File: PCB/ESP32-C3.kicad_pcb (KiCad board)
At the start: 2 copper layers, 29.1 x 19.5 mm, 41 parts, among them J1 BattConn+, J2 BattConn-, SW1 TAK_6mm_THT, U1 USB-C-16P-SMD, U2 XT4052K421MR-G, U3 ESP32-C3, U4 RS3236-3.3YF5, X1 DPS_I2C, Y1 40MHz_S3240000151040

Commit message: gerber erstellt
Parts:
- X1: footprint Connector_PinHeader_2.54mm:PinHeader_1x04_P2.54mm_Vertical -> Connector_JST:JST_PH_B4B-PH-K_1x04_P2.00mm_Vertical
- moved AE1 1.15 mm to (121.0, 66.9)
- moved X1 0.05 mm to (109.3, 64.3), turned to 0 degrees
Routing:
- net Net-(AE1-Pad1): track 10.4 -> 11.6 mm

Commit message: update
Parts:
- moved C8 0.20 mm to (103.0, 65.2)
- moved C14 0.10 mm to (109.2, 72.3)
- moved R2 0.10 mm to (102.0, 71.8)
- moved D3 0.10 mm to (105.6, 65.1)
- moved R4 0.10 mm to (105.2, 70.1)
- moved R5 0.10 mm to (103.2, 70.1)
- moved U2 0.10 mm to (104.2, 67.8)
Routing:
- net EXTI: track 36.1 -> 33.6 mm
- net GND: track 45.1 -> 45.2 mm, vias 19 -> 41

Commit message: update to KiCad 7
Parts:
- X1: moved to B.Cu

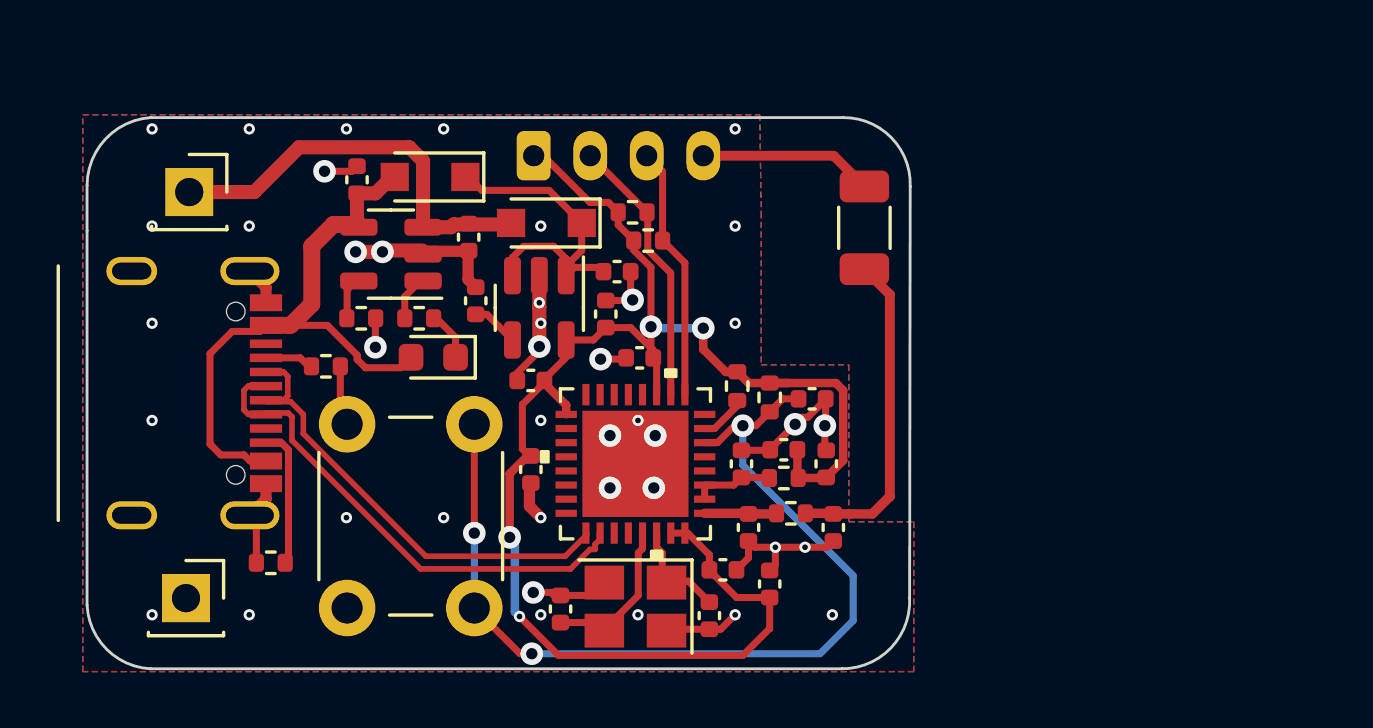
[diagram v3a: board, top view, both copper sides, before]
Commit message: updated the charging circuit
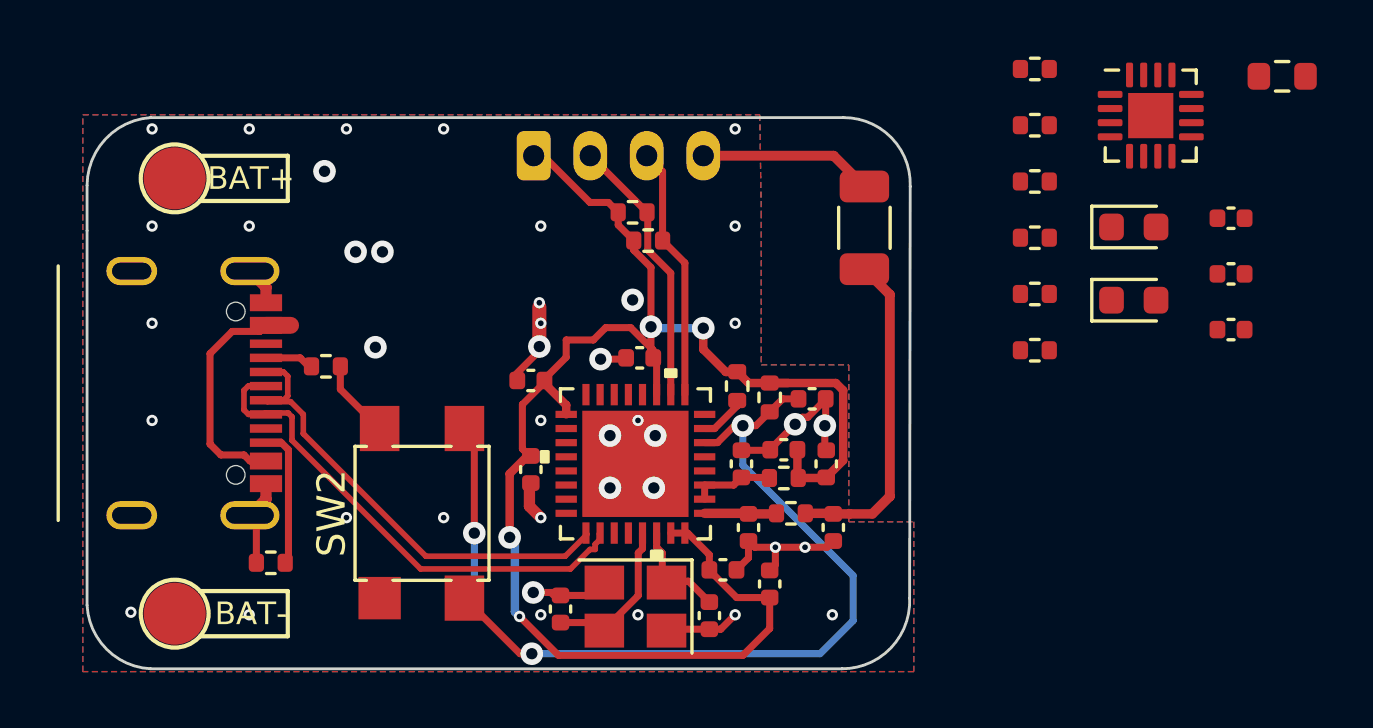
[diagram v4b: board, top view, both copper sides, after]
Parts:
- removed C10, C18: 1u_0402_X5R_25V, Capacitor_SMD:C_0402_1005Metric
- removed C13: 10n_0402_X7R_50V, Capacitor_SMD:C_0402_1005Metric
- removed C8: 4u7_0402_X5R_10V, Capacitor_SMD:C_0402_1005Metric
- removed C9: 10u_0402_X5R_6V3, Capacitor_SMD:C_0402_1005Metric
- removed D1: 0603_RED, LED_SMD:LED_0603_1608Metric
- removed D2, D3: 1N5819WS(Basic), Diode_SMD:D_SOD-323_HandSoldering
- removed J1: BattConn+, Connector_PinSocket_2.54mm:PinSocket_1x01_P2.54mm_Vertical
- removed J2: BattConn-, Connector_PinSocket_2.54mm:PinSocket_1x01_P2.54mm_Vertical
- removed R4, R5: 3k3_0402, Resistor_SMD:R_0402_1005Metric
- removed SW1: TAK_6mm_THT, Button_Switch_THT:SW_PUSH_6mm_H5mm
- removed U4: RS3236-3.3YF5, Package_TO_SOT_SMD:SOT-23-5
- added C19: 1u_0402_X5R_25V, Capacitor_SMD:C_0402_1005Metric, F.Cu at (134.0, 66.6)
- added C20: 4u7_0402_X5R _10V, Capacitor_SMD:C_0402_1005Metric, F.Cu at (134.0, 68.5)
- added C21: 4u7_0402_X5R _10V, Capacitor_SMD:C_0402_1005Metric, F.Cu at (134.0, 70.5)
- added D4: 0603_GREEN, LED_SMD:LED_0603_1608Metric, F.Cu at (130.5, 66.9)
- added D5: 0603_RED, LED_SMD:LED_0603_1608Metric, F.Cu at (130.5, 69.5)
- added R10: 2k0_0402, Resistor_SMD:R_0402_1005Metric, F.Cu at (127.0, 63.3)
- added R11: 549k_1_0402, Resistor_SMD:R_0402_1005Metric, F.Cu at (127.0, 65.3)
- added R12: 1k_0402, Resistor_SMD:R_0402_1005Metric, F.Cu at (127.0, 67.2)
- added R13: 3k_0402_ntc, Resistor_SMD:R_0402_1005Metric, F.Cu at (127.0, 69.2)
- added R14: 1k8_5_0402, Resistor_SMD:R_0402_1005Metric, F.Cu at (127.0, 71.2)
- added R15: 1k5_0603, Resistor_SMD:R_0603_1608Metric, F.Cu at (135.8, 61.5)
- added R9: 2k0_0402, Resistor_SMD:R_0402_1005Metric, F.Cu at (127.0, 61.3)
- added SW2: TS4535TP 250gf 009, switch:SW_SPST_TL3305B, F.Cu at (105.3, 77.0)
- added TP1: BAT+, testpoints:TP3, F.Cu at (96.6, 65.2)
- added TP2: BAT-, testpoints:TP3, F.Cu at (96.6, 80.5)
- U2: value XT4052K421MR-G -> BQ24072RGT; footprint Package_TO_SOT_SMD:TSOT-23-5 -> Package_DFN_QFN:VQFN-16-1EP_3x3mm_P0.5mm_EP1.6x1.6mm
- moved U2 27.3 mm to (131.1, 62.9), turned to 0 degrees
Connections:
- U2 pad 2: GND -> +BATT
- U2 pad 4: VCC -> GND
- U2 pad 5: Net-(R5-Pad1) -> +3.3V
- U3 pad 14: unconnected-(U3-Pad14) -> GPIO8
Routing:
- net +BATT: track 14.8 -> 0.00 mm
- net VCC: track 21.7 -> 8.69 mm
- net Net-(C10-Pad1): track 11.9 -> 0.00 mm
- net GND: track 45.2 -> 35.0 mm
- net Net-(D1-Pad1): track 1.80 -> 0.00 mm
- net Net-(C13-Pad1): track 1.68 -> 0.00 mm
- net Net-(U2-TS): track 1.59 -> 0.00 mm
- net Net-(R5-Pad1): track 1.50 -> 0.00 mm

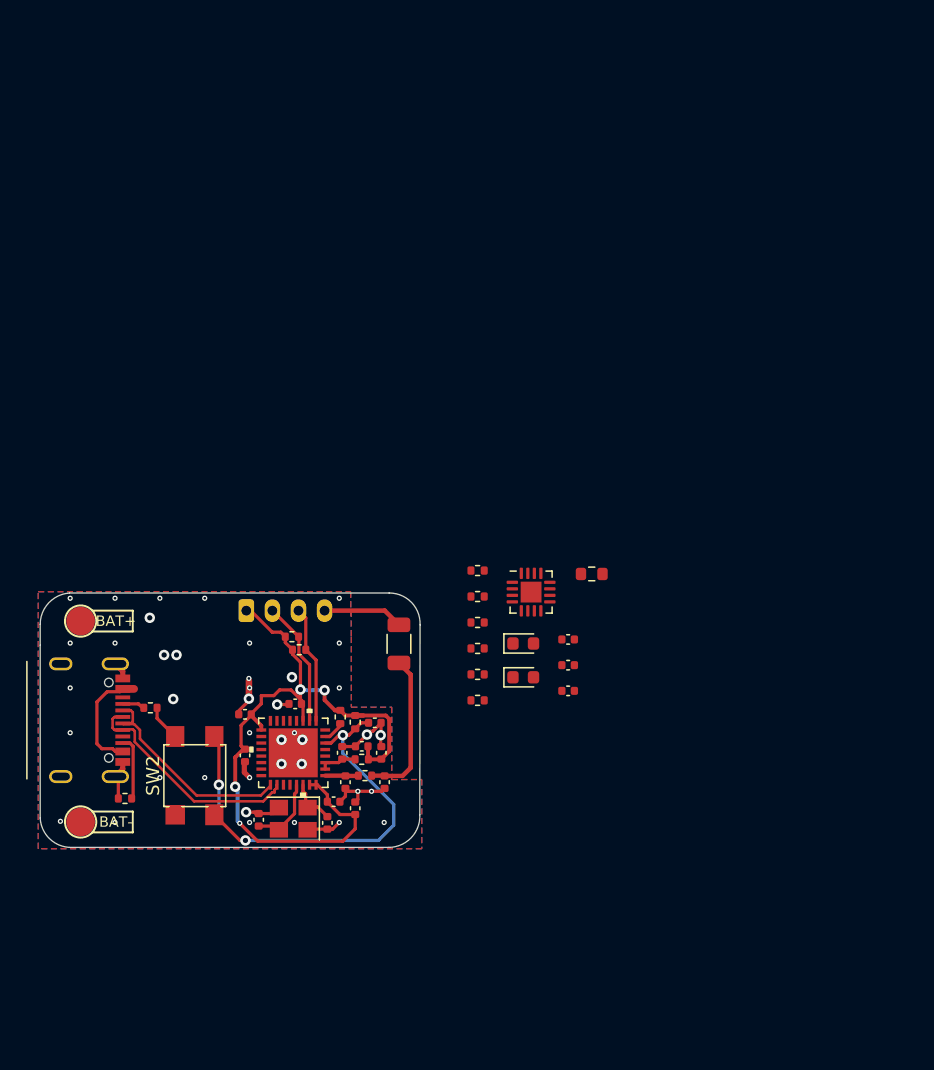
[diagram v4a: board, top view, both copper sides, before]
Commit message: Mit dem Layout angefangen
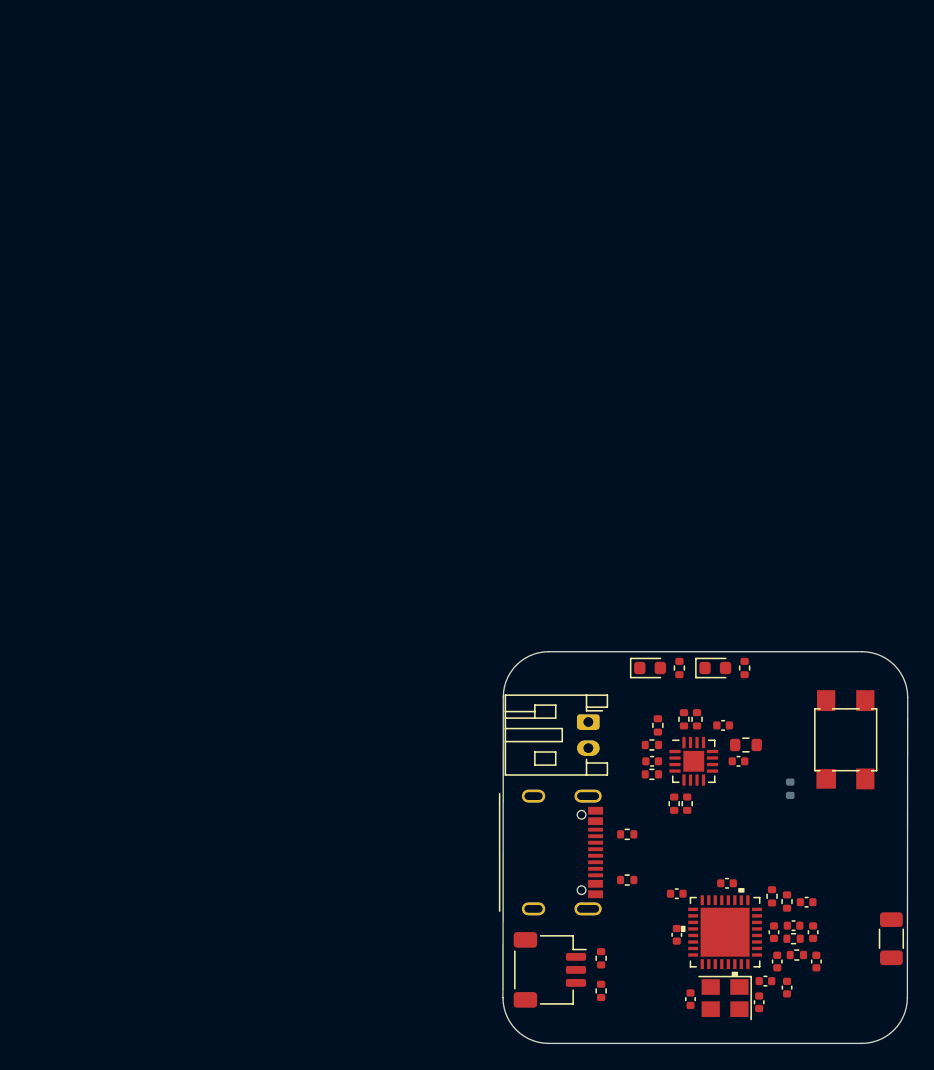
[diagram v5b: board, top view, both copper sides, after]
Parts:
- removed TP1: BAT+, testpoints:TP3
- removed TP2: BAT-, testpoints:TP3
- removed X1: DPS_I2C, Connector_JST:JST_PH_B4B-PH-K_1x04_P2.00mm_Vertical
- added J1: HCZZ0039-3, Connector_JST:JST_SH_SM03B-SRSS-TB_1x03-1MP_P1.00mm_Horizontal, F.Cu at (132.6, 91.9)
- added J2: DPS_PPS_Right_Angle, Connector_JST:JST_PH_S2B-PH-K_1x02_P2.00mm_Horizontal, F.Cu at (135.5, 72.9)
- added R16: 5k1_0402, Resistor_SMD:R_0402_1005Metric, F.Cu at (143.1, 79.2)
- added R17: 5k1_0402, Resistor_SMD:R_0402_1005Metric, F.Cu at (142.1, 79.2)
- added R4: 5k1_0402, Resistor_SMD:R_0402_1005Metric, F.Cu at (140.4, 76.9)
- added R5: 5k1_0402, Resistor_SMD:R_0402_1005Metric, F.Cu at (143.8, 72.7)
- R13: moved to B.Cu
- moved SW2 50.0 mm to (155.2, 74.2)
- moved AE1 44.0 mm to (158.8, 89.5)
- moved R3 39.0 mm to (138.5, 85.0), turned to 0 degrees
- moved R2 37.8 mm to (138.5, 81.5)
- moved U1 37.6 mm to (131.3, 82.9)
- moved R8 36.0 mm to (136.5, 93.5), turned to -90 degrees
- moved C11 35.8 mm to (142.3, 89.2)
- moved C14 35.8 mm to (142.3, 86.0)
- moved C16 35.8 mm to (148.6, 94.4)
- moved C5 35.8 mm to (146.2, 85.2)
- moved C1 35.8 mm to (152.2, 86.7)
- moved C12 35.8 mm to (149.1, 92.8)
- moved C15 35.8 mm to (150.8, 93.2)
- moved C17 35.8 mm to (143.3, 94.1)
- moved C2 35.8 mm to (151.2, 88.5)
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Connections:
- net GPIO8 renamed TD
- D4 pad 1: Net-(D4-K) -> NPGOOD
- D5 pad 1: Net-(D5-K) -> NCHG
- U2 pad 14: GND -> TMR
- U2 pad 4: GND -> NCE
- U2 pad 5: +3.3V -> EN2
- U2 pad 6: GND -> EN1
- U2 pad 7: Net-(D4-K) -> NPGOOD
- U2 pad 9: Net-(D5-K) -> NCHG
- U3 pad 15: unconnected-(U3-GPIO9-Pad15) -> NCE
- U3 pad 16: unconnected-(U3-GPIO10-Pad16) -> TMR
- U3 pad 19: unconnected-(U3-SPIHD-Pad19) -> NPGOOD
- U3 pad 20: unconnected-(U3-SPIWP-Pad20) -> NCHG
- U3 pad 21: unconnected-(U3-SPICS0-Pad21) -> EN2
- U3 pad 22: unconnected-(U3-SPICLK-Pad22) -> EN1
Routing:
- net +3.3V: track 57.2 -> 0.00 mm, vias 4 -> 0
- net GND: track 35.0 -> 0.00 mm, vias 41 -> 0
- net EXTI: track 33.6 -> 0.00 mm, vias 3 -> 0
- net USB_D+: track 17.8 -> 0.00 mm
- net USB_D-: track 16.8 -> 0.00 mm
- net Net-(AE1-A): track 11.7 -> 0.00 mm
- net MCU_SDA: track 9.64 -> 0.00 mm
- net MCU_SCL: track 9.01 -> 0.00 mm
- net VCC: track 8.69 -> 0.00 mm
- net Net-(U3-XTAL_N): track 5.43 -> 0.00 mm
- net Net-(U1-CC2): track 4.94 -> 0.00 mm
- net Net-(U3-XTAL_P): track 3.75 -> 0.00 mm
- net Net-(C7-Pad2): track 2.91 -> 0.00 mm
- net Net-(U3-LNA_IN): track 2.56 -> 0.00 mm
- net Net-(U1-CC1): track 1.78 -> 0.00 mm
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- removed copper zone on B.Cu, net GND
- removed copper zone on F.Cu, net GND
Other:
- board size 29.1 x 19.5 mm -> 31 x 30 mm

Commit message: Layout weiter gemacht.
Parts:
- U3: footprint ESP32-C3:ESP32-C3 -> Package_DFN_QFN:QFN-32-1EP_5x5mm_P0.5mm_EP3.7x3.7mm
- moved R13 11.4 mm to (140.6, 82.6), turned to -90 degrees
- moved D4 7.31 mm to (133.0, 69.7)
- moved D5 7.31 mm to (138.0, 69.7)
- moved R10 7.31 mm to (135.2, 69.7)
- moved R9 7.31 mm to (140.2, 69.7)
- moved AE1 4.47 mm to (154.3, 89.9)
- moved SW2 3.82 mm to (151.5, 73.5)
- moved C14 2.42 mm to (140.0, 86.8), turned to 90 degrees
- moved R1 2.33 mm to (148.4, 86.3)
- moved Y1 2.30 mm to (143.7, 94.2)
- moved C1 2.30 mm to (149.9, 86.8)
- moved C11 2.30 mm to (140.0, 89.3)
- moved C12 2.30 mm to (146.8, 92.8)
- moved C15 2.30 mm to (148.4, 93.3)
- moved C16 2.30 mm to (146.3, 94.5)
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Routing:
- net +3.3V: track 0.00 -> 84.9 mm, vias 0 -> 4
- net GND: track 0.00 -> 38.2 mm, vias 0 -> 26
- net VCC: track 0.00 -> 38.0 mm
- net MCU_SDA: track 0.00 -> 33.4 mm, vias 0 -> 2
- net MCU_SCL: track 0.00 -> 31.2 mm, vias 0 -> 2
- net EXTI: track 0.00 -> 21.9 mm
- net NCHG: track 0.00 -> 18.5 mm
- net NPGOOD: track 0.00 -> 18.1 mm
- net USB_D+: track 0.00 -> 17.3 mm
- net USB_D-: track 0.00 -> 16.4 mm
- net Net-(R12-Pad2): track 0.00 -> 9.91 mm, vias 0 -> 1
- net +BATT: track 0.00 -> 7.20 mm
- net Net-(U3-XTAL_N): track 0.00 -> 5.68 mm
- net Net-(U3-XTAL_P): track 0.00 -> 3.70 mm
- net Net-(C7-Pad2): track 0.00 -> 2.91 mm
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- added copper zone on B.Cu, net GND
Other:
- board size 31 x 30 mm -> 26.7 x 27.8 mm

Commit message: updated
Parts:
- removed R14: 1k8_5_0402, Resistor_SMD:R_0402_1005Metric
- added R18: 8k2_0402, Resistor_SMD:R_0402_1005Metric, F.Cu at (141.4, 72.2)
- AE1: footprint Resistor_SMD:R_1206_3216Metric -> RF_Antenna:Texas_SWRA117D_2.4GHz_Left
- moved C11 4.35 mm to (140.2, 85.0), turned to 90 degrees
- moved AE1 2.86 mm to (151.6, 90.8), turned to -90 degrees
- moved C14 2.21 mm to (141.2, 85.0)
- moved R2 1.04 mm to (137.7, 80.9), turned to 90 degrees
- moved R5 0.35 mm to (143.0, 72.2)
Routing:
- net +3.3V: track 84.9 -> 114.4 mm, vias 4 -> 9
- net TMR: track 1.27 -> 22.7 mm, vias 0 -> 2
- net NCHG: track 18.5 -> 37.9 mm, vias 0 -> 2
- net EN1: track 1.41 -> 19.7 mm, vias 0 -> 2
- net EN2: track 1.67 -> 18.2 mm, vias 0 -> 2
- net TD: track 0.00 -> 16.1 mm, vias 0 -> 2
- net NCE: track 1.37 -> 14.3 mm, vias 0 -> 2
- net NPGOOD: track 18.1 -> 29.6 mm, vias 0 -> 2
- net EXTI: track 21.9 -> 28.6 mm
- net GND: track 38.2 -> 41.9 mm, vias 26 -> 31
- net Net-(U3-LNA_IN): track 0.00 -> 2.56 mm
- net Net-(AE1-A): track 0.00 -> 1.91 mm
- added copper zone on F.Cu, net GND
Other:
- board size 26.7 x 27.8 mm -> 28.4 x 27.8 mm
